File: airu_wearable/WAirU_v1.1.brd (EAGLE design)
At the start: 43.8 x 51.7 mm, 57 parts, among them Q1 BSS123, Q2 MMBT3904LT1G, Q3 MMBT3904LT1G, Q4 BSS84, U1 19-237A/BHR6GHC-M01/2T, U2 CN3065-DFN8, U3 HDC1080DMBT, U4 PAM2305AABADJ, U6 PAM2401, U7 ESP32_WROOM32_SKINNY

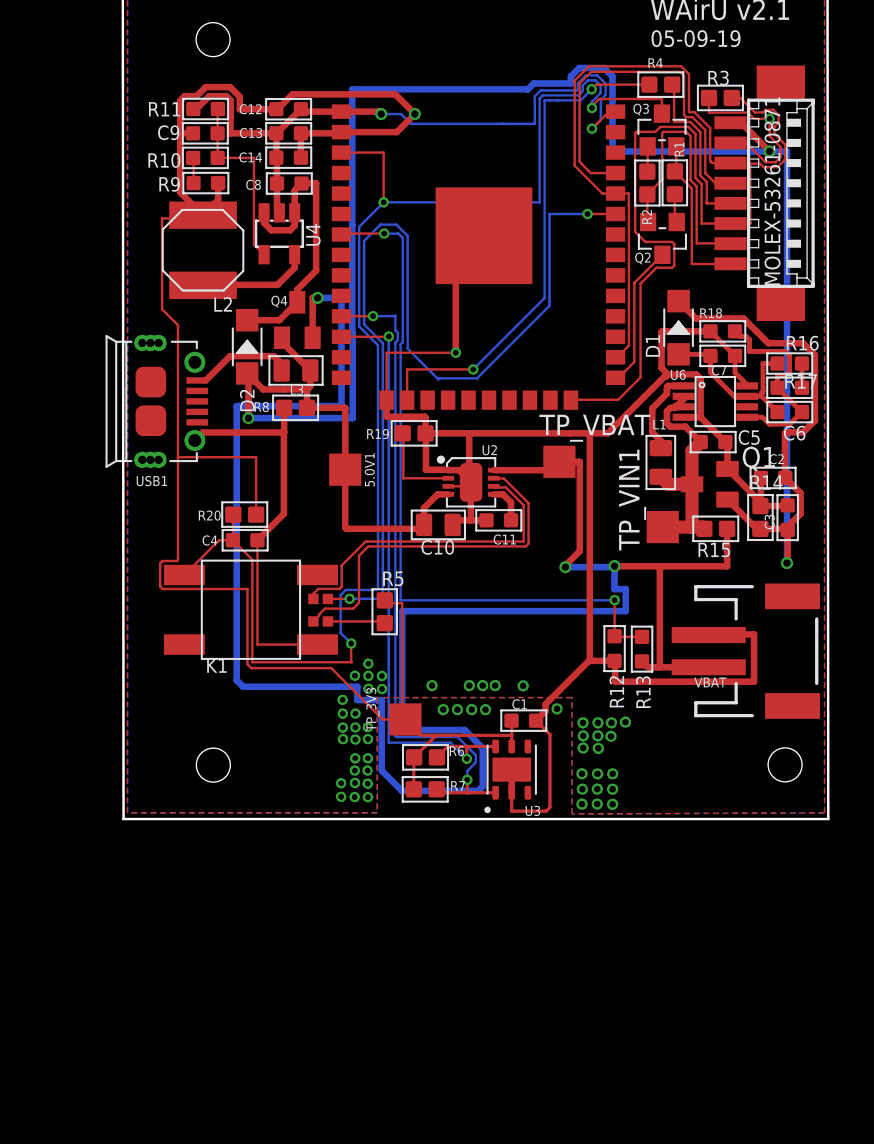
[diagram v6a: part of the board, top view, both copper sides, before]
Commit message: new issue (#16) opened. Remade PAM2401 circuit.
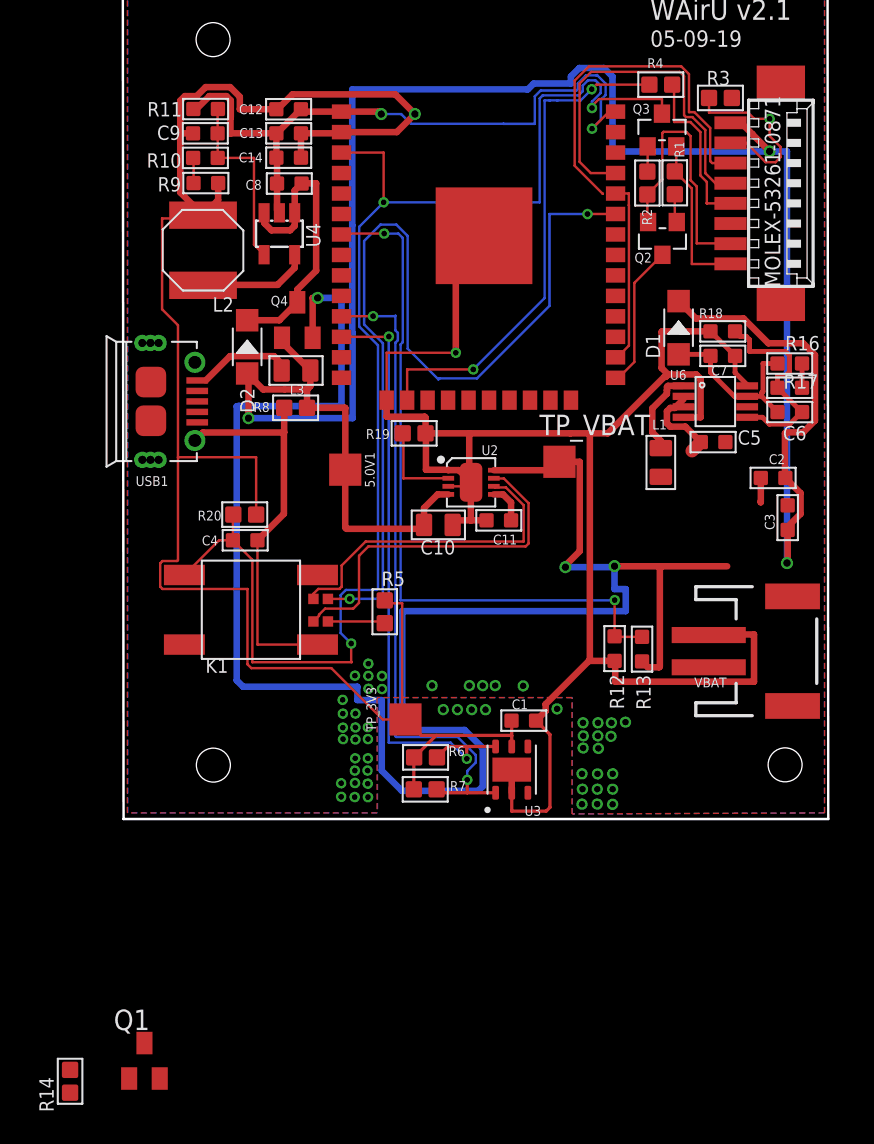
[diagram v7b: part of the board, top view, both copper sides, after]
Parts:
- removed R15: 100K 1/10W, Seeed-Resistor:R0603
- removed TP_VIN1: TPTP20SQ, testpad:TP20SQ
- Q1: value BSS123 -> BSS84; device transistor-small-signal:SOT23 -> BSS84:SOT23
- moved R14 55.3 mm to (4.66, -17.8)
- moved Q1 50.1 mm to (9.27, -16.6), turned to 0 degrees
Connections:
- removed net PM_RESET: MOLEX-53261-0871.3, R3.2, U7.24
- removed net PM_SET/RXD0: MOLEX-53261-0871.6, U7.26, U7.34
- new net EN_PAM2401: Q1.2, U7.24
- new net N$7: Q1.3, R14.2, U6.2
- new net PM_SET: MOLEX-53261-0871.6, R3.2, U7.26
- new net RXD0: MOLEX-53261-0871.3, U7.34
- net GND: no longer Q1.2
- net VBAT: no longer R15.2
- net VBUS: no longer R14.2
- net V_IN1: no longer Q1.3, R15.1, TP_VIN1.TP, U6.2
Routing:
- net PM_RESET: track 49.1 -> 0.00 mm
- net PM_SET/RXD0: track 35.0 -> 0.00 mm
- net PM_SET: track 0.00 -> 34.3 mm
- net V_IN1: track 15.1 -> 5.45 mm
- net GND: track 203.4 -> 194.7 mm
- net VBAT: track 128.5 -> 123.1 mm
- net VBUS: track 147.5 -> 143.0 mm

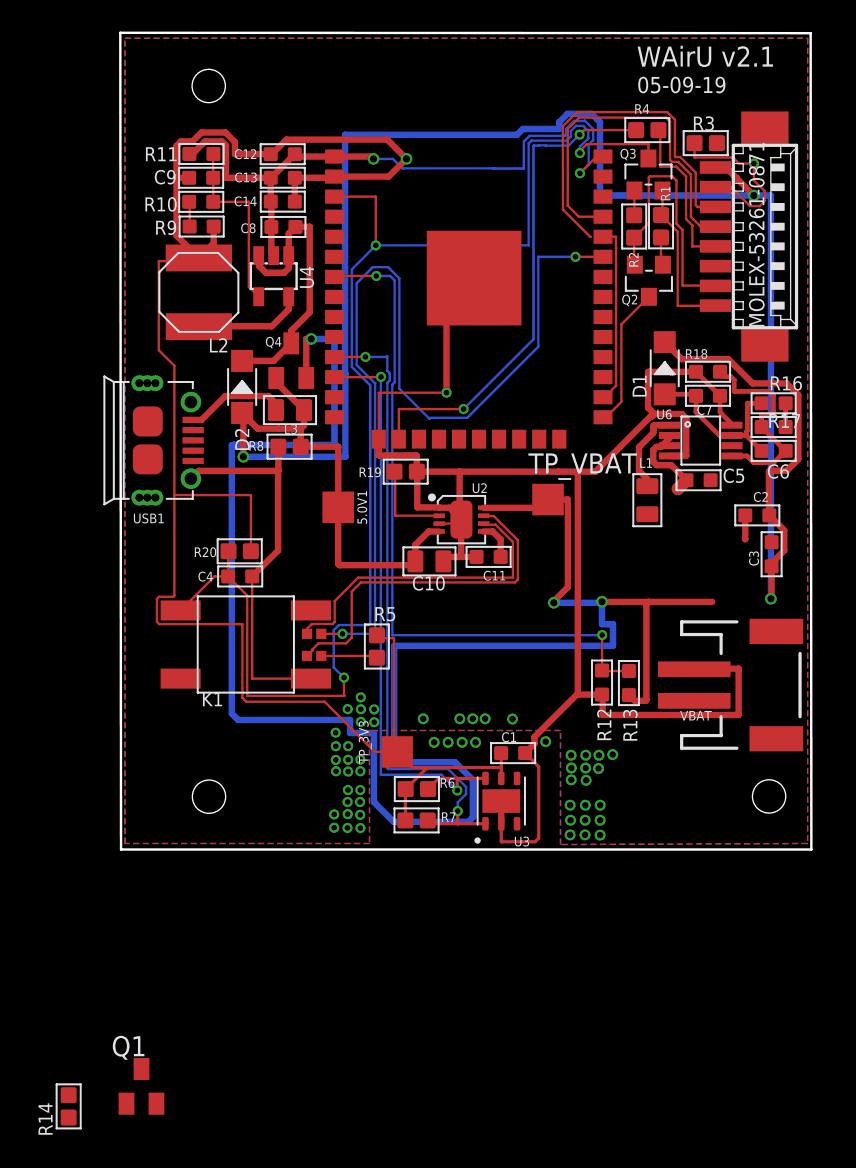
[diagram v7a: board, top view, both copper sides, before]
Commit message: Draw PCB plus dimension for WAirU 2.1 Export BOM list Included PCB pdf for future references
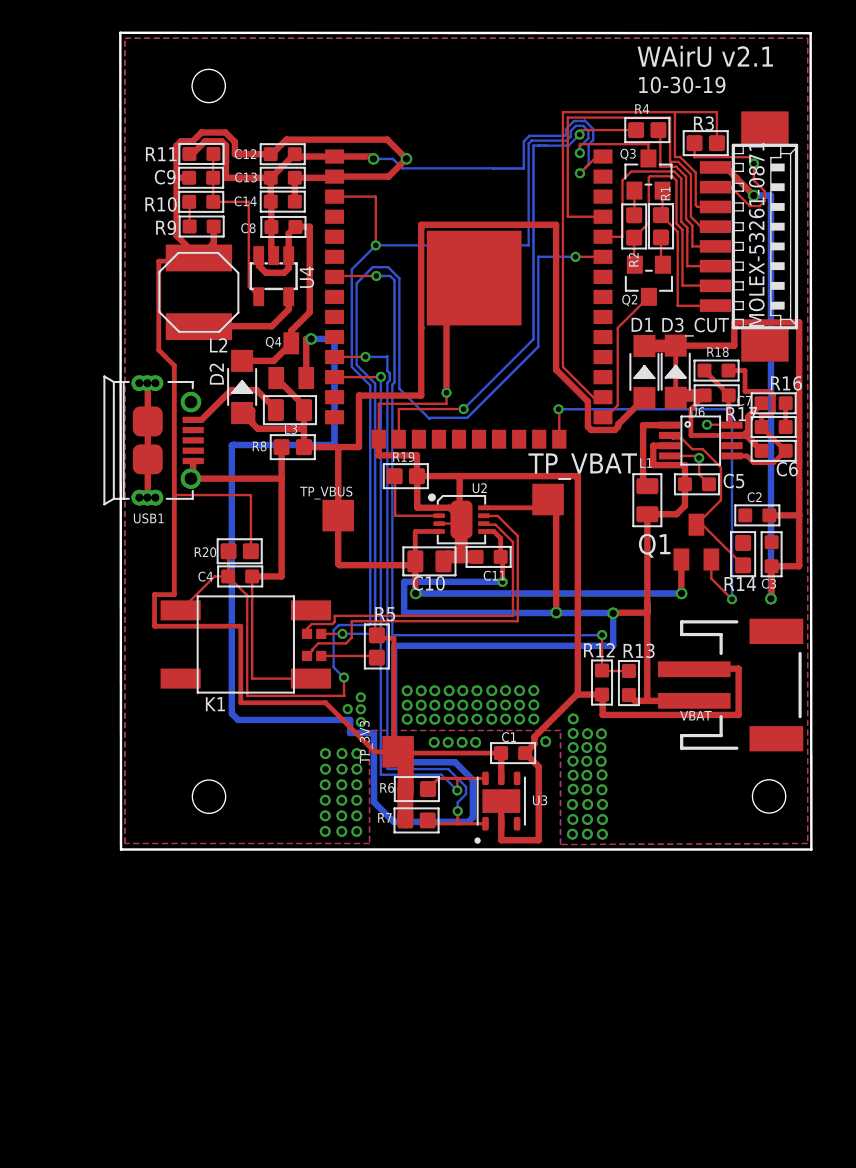
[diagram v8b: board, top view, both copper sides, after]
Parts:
- removed 5.0V1: TPTP20SQ, testpad:TP20SQ
- added D3_CUT: 20V-1A, Seeed-OPL-Diode:SOD-123
- added TP_VBUS: TPTP20SQ, testpad:TP20SQ
- moved R14 55.2 mm to (47.4, 17.1)
- moved Q1 49.2 mm to (44.4, 17.9)
- moved D1 1.31 mm to (41.1, 28.7)
- moved C7 0.55 mm to (45.7, 27.2)
- moved R18 0.54 mm to (45.7, 28.8)
- moved R19 0.28 mm to (26.0, 22.1)
- moved C5 0.28 mm to (44.5, 21.6)
- moved R8 0.21 mm to (18.9, 23.9)
- moved TP_3V3 0.06 mm to (25.5, 4.62)
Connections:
- removed net N$4: C6.2, C7.2, D1.+, R16.1, U6.7
- removed net V_IN1: C5.2, L1.1, U6.3
- new net 5.0V: C2.2, C3.2, D1.-, D3_CUT.-, MOLEX-53261-0871.8
- new net PAM2401_OUT: C6.2, C7.2, D3_CUT.+, R16.1, U6.7
- net VBAT: now also C5.2, L1.1, U6.3
- net VBUS: now also D1.+, TP_VBUS.TP; no longer 5.0V1.TP, C2.2, C3.2, D1.-, MOLEX-53261-0871.8
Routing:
- net 5.0V: track 0.00 -> 62.8 mm, vias 0 -> 2
- net VBUS: track 143.0 -> 96.5 mm, vias 3 -> 2
- net VBAT: track 123.1 -> 155.1 mm, vias 3 -> 4
- net EN_PAM2401: track 0.00 -> 27.8 mm, vias 0 -> 2
- net RXD0: track 0.00 -> 16.4 mm
- net PAM2401_OUT: track 0.00 -> 15.8 mm
- net N$7: track 0.00 -> 13.6 mm
- net N$4: track 11.8 -> 0.00 mm, vias 0 -> 1
- net V_IN1: track 5.45 -> 0.00 mm
- net PM_SET: track 34.3 -> 39.2 mm
- net TXD0: track 22.9 -> 24.0 mm
- net CHG_DONE: track 20.1 -> 20.9 mm
- net 3.3V: track 114.7 -> 115.5 mm
- net CHARGING: track 22.4 -> 23.0 mm
- net GND: track 194.7 -> 194.2 mm, vias 4 -> 6
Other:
- board text added: "10-30-19"
- board text removed: "05-09-19"
